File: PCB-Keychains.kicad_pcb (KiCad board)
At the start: 2 copper layers, 13 parts

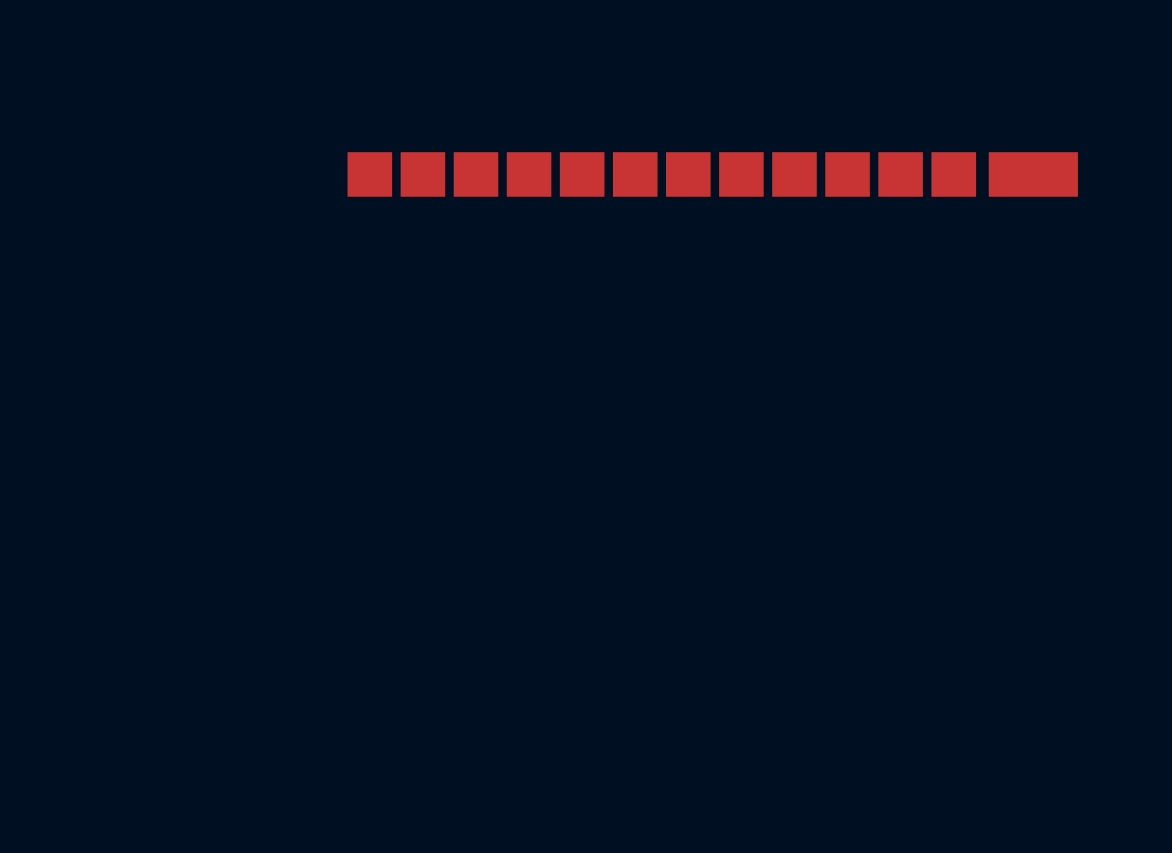
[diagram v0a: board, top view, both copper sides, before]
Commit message: Make tiny keychains, then realize it is too small
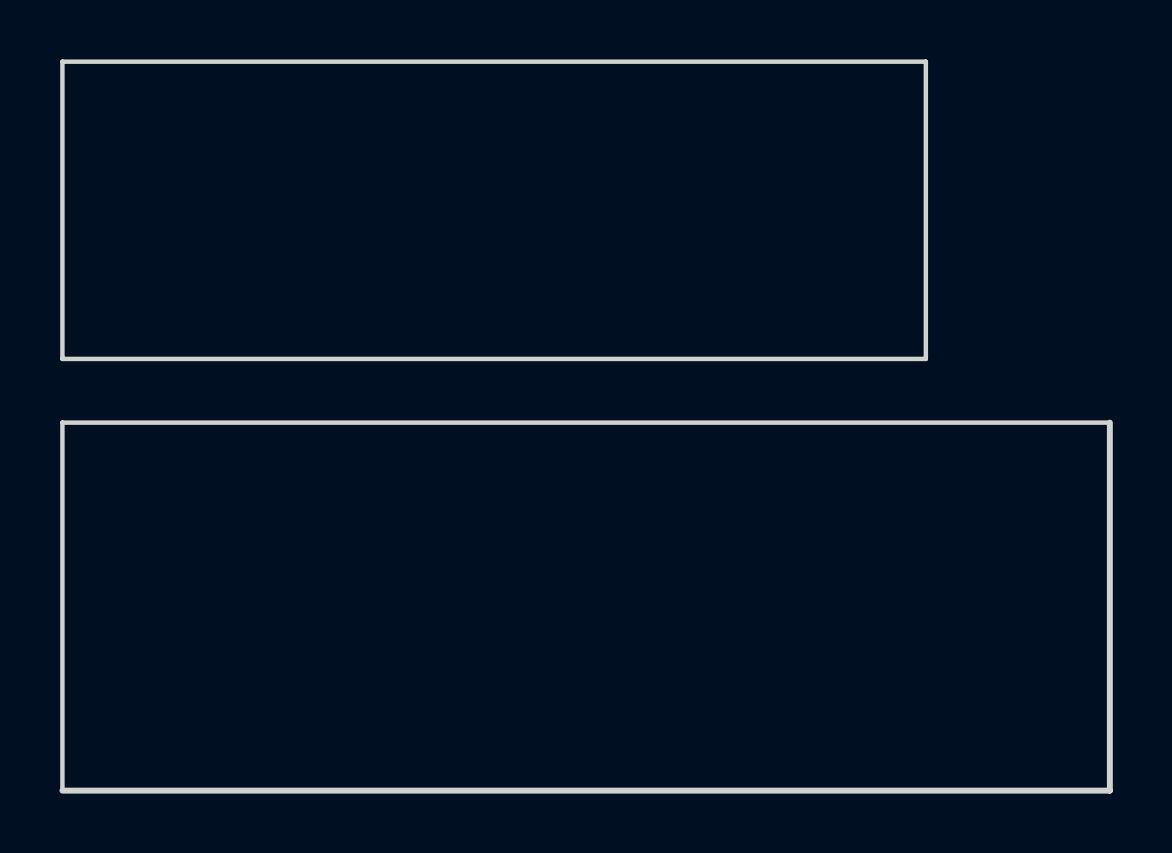
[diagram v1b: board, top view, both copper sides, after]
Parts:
- removed the REF** at (30.6, 21.7)
- removed the REF** at (46.7, 21.7)
- removed the REF** at (48.4, 21.7)
- removed the REF** at (50.2, 21.7)
- removed the REF** at (52.9, 21.7)
- removed the REF** at (32.4, 21.7)
- removed the REF** at (34.2, 21.7)
- removed the REF** at (35.9, 21.7)
- removed the REF** at (37.7, 21.7)
- removed the REF** at (39.5, 21.7)
- removed the REF** at (41.3, 21.7)
- removed the REF** at (43.1, 21.7)
- removed the REF** at (44.9, 21.7)
- added REF**: Pad-1U, locallib:Pad-1U, F.Cu at (42.4, 31.2)
- added REF**: Pad-1U, locallib:Pad-1U, F.Cu at (33.8, 31.2)
- added REF**: Pad-1U, locallib:Pad-1U, F.Cu at (34.3, 22.9)
- added REF**: Pad-1U, locallib:Pad-1U, F.Cu at (38.1, 22.9)
- added REF**: Pad-1U, locallib:Pad-1U, F.Cu at (40.0, 22.9)
- added REF**: Pad-1U, locallib:Pad-1U, F.Cu at (24.8, 22.9)
- added REF**: Pad-1U, locallib:Pad-1U, F.Cu at (30.5, 22.9)
- added REF**: Pad-1U, locallib:Pad-1U, F.Cu at (28.6, 22.9)
- added REF**: Pad-1U, locallib:Pad-1U, F.Cu at (26.7, 22.9)
- added REF**: Pad-1U, locallib:Pad-1U, F.Cu at (41.9, 22.9)
- added REF**: Pad-1U, locallib:Pad-1U, F.Cu at (43.8, 22.9)
- added REF**: Pad-1U, locallib:Pad-1U, F.Cu at (21.4, 19.1)
- added REF**: Pad-1U, locallib:Pad-1U, F.Cu at (37.6, 31.2)
- added REF**: Pad-1U, locallib:Pad-1U, F.Cu at (23.3, 19.1)
- added REF**: Pad-1U, locallib:Pad-1U, F.Cu at (25.2, 19.1)
- added REF**: Pad-1U, locallib:Pad-1U, F.Cu at (27.1, 19.1)
- added REF**: Pad-1U, locallib:Pad-1U, F.Cu at (29.1, 19.1)
- added REF**: Pad-1U, locallib:Pad-1U, F.Cu at (31.0, 19.1)
- added REF**: Pad-1U, locallib:Pad-1U, F.Cu at (32.9, 19.1)
- added REF**: Pad-1U, locallib:Pad-1U, F.Cu at (34.8, 19.1)
- added REF**: Pad-1U, locallib:Pad-1U, F.Cu at (36.7, 19.1)
- added REF**: Pad-1U, locallib:Pad-1U, F.Cu at (38.6, 19.1)
- added REF**: Pad-1U, locallib:Pad-1U, F.Cu at (40.5, 19.1)
- added REF**: Pad-1U, locallib:Pad-1U, F.Cu at (39.5, 31.2)
- added REF**: Pad-1U, locallib:Pad-1U, F.Cu at (42.4, 19.1)
- added REF**: Pad-1U, locallib:Pad-1U, F.Cu at (44.3, 19.1)
- added REF**: Pad-2U, locallib:Pad-2U, F.Cu at (47.1, 19.1)
- added REF**: Pad-1.5U, locallib:Pad-1.5U, F.Cu at (21.9, 21.0)
- added REF**: Pad-1U, locallib:Pad-1U, F.Cu at (24.3, 21.0)
- added REF**: Pad-1U, locallib:Pad-1U, F.Cu at (26.2, 21.0)
- added REF**: Pad-1U, locallib:Pad-1U, F.Cu at (28.1, 21.0)
- added REF**: Pad-1U, locallib:Pad-1U, F.Cu at (30.0, 21.0)
- added REF**: Pad-1U, locallib:Pad-1U, F.Cu at (31.9, 21.0)
- added REF**: Pad-1U, locallib:Pad-1U, F.Cu at (33.8, 21.0)
- added REF**: Pad-1U, locallib:Pad-1U, F.Cu at (29.1, 31.2)
- added REF**: Pad-1U, locallib:Pad-1U, F.Cu at (35.7, 21.0)
- added REF**: Pad-1U, locallib:Pad-1U, F.Cu at (37.6, 21.0)
- added REF**: Pad-1U, locallib:Pad-1U, F.Cu at (39.5, 21.0)
- added REF**: Pad-1U, locallib:Pad-1U, F.Cu at (41.4, 21.0)
- added REF**: Pad-1U, locallib:Pad-1U, F.Cu at (43.3, 21.0)
- added REF**: Pad-1U, locallib:Pad-1U, F.Cu at (45.2, 21.0)
- added REF**: Pad-1.5U, locallib:Pad-1.5U, F.Cu at (47.6, 21.0)
- added REF**: Pad-1.75U, locallib:Pad-1.75U, F.Cu at (22.1, 22.9)
- added REF**: Pad-2.25U, locallib:Pad-2.25U, F.Cu at (46.9, 22.9)
- added REF**: Pad-2.25U, locallib:Pad-2.25U, F.Cu at (22.6, 24.8)
- added REF**: Pad-1U, locallib:Pad-1U, F.Cu at (31.0, 31.2)
- added REF**: Pad-2.75U, locallib:Pad-2.75U, F.Cu at (46.4, 24.8)
- added REF**: Pad-1.5U, locallib:Pad-1.5U, F.Cu at (21.9, 26.7)
- added REF**: Pad-1U, locallib:Pad-1U, F.Cu at (24.3, 26.7)
- added REF**: Pad-1.5U, locallib:Pad-1.5U, F.Cu at (26.7, 26.7)
- added REF**: Pad-7U, locallib:Pad-7U, F.Cu at (34.8, 26.7)
- added REF**: Pad-1U, locallib:Pad-1U, F.Cu at (35.7, 31.2)
- added REF**: Pad-1U, locallib:Pad-1U, F.Cu at (21.4, 31.2)
- added REF**: Pad-1U, locallib:Pad-1U, F.Cu at (54.3, 41.2)
- added REF**: Pad-1U, locallib:Pad-1U, F.Cu at (52.4, 41.2)
- added REF**: Pad-1U, locallib:Pad-1U, F.Cu at (50.5, 41.2)
- added REF**: Pad-1U, locallib:Pad-1U, F.Cu at (44.3, 31.2)
- added REF**: Pad-1U, locallib:Pad-1U, F.Cu at (52.4, 39.3)
- added REF**: Pad-1U, locallib:Pad-1U, F.Cu at (54.3, 35.5)
- added REF**: Pad-1U, locallib:Pad-1U, F.Cu at (52.4, 35.5)
- added REF**: Pad-1U, locallib:Pad-1U, F.Cu at (50.5, 35.5)
- added REF**: Pad-1U, locallib:Pad-1U, F.Cu at (54.3, 33.6)
- added REF**: Pad-1U, locallib:Pad-1U, F.Cu at (52.4, 33.6)
- added REF**: Pad-1U, locallib:Pad-1U, F.Cu at (50.5, 33.6)
- added REF**: Pad-1U, locallib:Pad-1U, F.Cu at (44.3, 33.6)
- added REF**: Pad-1U, locallib:Pad-1U, F.Cu at (35.7, 35.5)
- added REF**: Pad-1U, locallib:Pad-1U, F.Cu at (31.9, 35.5)
- added REF**: Pad-1U, locallib:Pad-1U, F.Cu at (46.2, 31.2)
- added REF**: Pad-1U, locallib:Pad-1U, F.Cu at (33.8, 35.5)
- added REF**: Pad-1U, locallib:Pad-1U, F.Cu at (37.6, 35.5)
- added REF**: Pad-1U, locallib:Pad-1U, F.Cu at (39.5, 35.5)
- added REF**: Pad-1U, locallib:Pad-1U, F.Cu at (27.6, 39.3)
- added REF**: Pad-1U, locallib:Pad-1U, F.Cu at (33.3, 39.3)
- added REF**: Pad-1U, locallib:Pad-1U, F.Cu at (29.5, 39.3)
- added REF**: Pad-1U, locallib:Pad-1U, F.Cu at (41.0, 39.3)
- added REF**: Pad-1U, locallib:Pad-1U, F.Cu at (37.1, 39.3)
- added REF**: Pad-1U, locallib:Pad-1U, F.Cu at (42.9, 39.3)
- added REF**: Pad-1U, locallib:Pad-1U, F.Cu at (39.1, 39.3)
- added REF**: Pad-1U, locallib:Pad-1U, F.Cu at (48.1, 31.2)
- added REF**: Pad-1U, locallib:Pad-1U, F.Cu at (31.4, 39.3)
- added REF**: Pad-1U, locallib:Pad-1U, F.Cu at (25.7, 39.3)
- added REF**: Pad-1U, locallib:Pad-1U, F.Cu at (35.2, 39.3)
- added REF**: Pad-2.25U, locallib:Pad-2.25U, F.Cu at (22.6, 39.3)
- added REF**: Pad-2.75U, locallib:Pad-2.75U, F.Cu at (46.4, 39.3)
- added REF**: Pad-1U, locallib:Pad-1U, F.Cu at (24.3, 35.5)
- added REF**: Pad-1U, locallib:Pad-1U, F.Cu at (30.0, 35.5)
- added REF**: Pad-1U, locallib:Pad-1U, F.Cu at (28.1, 35.5)
- added REF**: Pad-1U, locallib:Pad-1U, F.Cu at (26.2, 35.5)
- added REF**: Pad-1U, locallib:Pad-1U, F.Cu at (27.1, 33.6)
- added REF**: Pad-1U, locallib:Pad-1U, F.Cu at (54.3, 31.2)
- added REF**: Pad-1U, locallib:Pad-1U, F.Cu at (32.9, 33.6)
- added REF**: Pad-1U, locallib:Pad-1U, F.Cu at (40.5, 33.6)
- added REF**: Pad-1U, locallib:Pad-1U, F.Cu at (31.0, 33.6)
- added REF**: Pad-1U, locallib:Pad-1U, F.Cu at (38.6, 33.6)
- added REF**: Pad-1U, locallib:Pad-1U, F.Cu at (36.7, 33.6)
- added REF**: Pad-1U, locallib:Pad-1U, F.Cu at (34.8, 33.6)
- added REF**: Pad-1U, locallib:Pad-1U, F.Cu at (29.1, 33.6)
- added REF**: Pad-1.5U, locallib:Pad-1.5U, F.Cu at (47.6, 35.5)
- added REF**: Pad-1U, locallib:Pad-1U, F.Cu at (45.2, 35.5)
- added REF**: Pad-1U, locallib:Pad-1U, F.Cu at (41.4, 35.5)
- added REF**: Pad-1U, locallib:Pad-1U, F.Cu at (52.4, 31.2)
- added REF**: Pad-1U, locallib:Pad-1U, F.Cu at (43.3, 35.5)
- added REF**: Pad-1.5U, locallib:Pad-1.5U, F.Cu at (21.9, 41.2)
- added REF**: Pad-1.5U, locallib:Pad-1.5U, F.Cu at (47.6, 41.2)
- added REF**: Pad-1.5U, locallib:Pad-1.5U, F.Cu at (42.9, 41.2)
- added REF**: Pad-1.5U, locallib:Pad-1.5U, F.Cu at (26.7, 41.2)
- added REF**: Pad-7U, locallib:Pad-7U, F.Cu at (34.8, 41.2)
- added REF**: Pad-1U, locallib:Pad-1U, F.Cu at (25.2, 33.6)
- added REF**: Pad-1U, locallib:Pad-1U, F.Cu at (42.4, 33.6)
- added REF**: Pad-1U, locallib:Pad-1U, F.Cu at (32.4, 37.4)
- added REF**: Pad-1U, locallib:Pad-1U, F.Cu at (24.8, 37.4)
- added REF**: Pad-1U, locallib:Pad-1U, F.Cu at (50.5, 31.2)
- added REF**: Pad-1U, locallib:Pad-1U, F.Cu at (41.9, 37.4)
- added REF**: Pad-1.75U, locallib:Pad-1.75U, F.Cu at (22.1, 37.4)
- added REF**: Pad-1U, locallib:Pad-1U, F.Cu at (40.0, 37.4)
- added REF**: Pad-1U, locallib:Pad-1U, F.Cu at (38.1, 37.4)
- added REF**: Pad-1U, locallib:Pad-1U, F.Cu at (34.3, 37.4)
- added REF**: Pad-1U, locallib:Pad-1U, F.Cu at (36.2, 37.4)
- added REF**: Pad-2.25U, locallib:Pad-2.25U, F.Cu at (46.9, 37.4)
- added REF**: Pad-1U, locallib:Pad-1U, F.Cu at (28.6, 37.4)
- added REF**: Pad-1U, locallib:Pad-1U, F.Cu at (30.5, 37.4)
- added REF**: Pad-1U, locallib:Pad-1U, F.Cu at (26.7, 37.4)
- added REF**: Pad-1U, locallib:Pad-1U, F.Cu at (27.1, 31.2)
- added REF**: Pad-1U, locallib:Pad-1U, F.Cu at (43.8, 37.4)
- added REF**: Pad-1U, locallib:Pad-1U, F.Cu at (23.3, 33.6)
- added REF**: Pad-1U, locallib:Pad-1U, F.Cu at (21.4, 33.6)
- added REF**: Pad-2U, locallib:Pad-2U, F.Cu at (47.1, 33.6)
- added REF**: Pad-1.5U, locallib:Pad-1.5U, F.Cu at (21.9, 35.5)
- added REF**: Pad-1.5U, locallib:Pad-1.5U, F.Cu at (42.9, 26.7)
- added REF**: Pad-1U, locallib:Pad-1U, F.Cu at (45.2, 26.7)
- added REF**: Pad-1.5U, locallib:Pad-1.5U, F.Cu at (47.6, 26.7)
- added REF**: Pad-1U, locallib:Pad-1U, F.Cu at (31.4, 24.8)
- added REF**: Pad-1U, locallib:Pad-1U, F.Cu at (41.0, 24.8)
- added REF**: Pad-1U, locallib:Pad-1U, F.Cu at (25.2, 31.2)
- added REF**: Pad-1U, locallib:Pad-1U, F.Cu at (39.1, 24.8)
- added REF**: Pad-1U, locallib:Pad-1U, F.Cu at (37.1, 24.8)
- added REF**: Pad-1U, locallib:Pad-1U, F.Cu at (33.3, 24.8)
- added REF**: Pad-1U, locallib:Pad-1U, F.Cu at (35.2, 24.8)
- added REF**: Pad-1U, locallib:Pad-1U, F.Cu at (27.6, 24.8)
- added REF**: Pad-1U, locallib:Pad-1U, F.Cu at (29.5, 24.8)
- added REF**: Pad-1U, locallib:Pad-1U, F.Cu at (25.7, 24.8)
- added REF**: Pad-1U, locallib:Pad-1U, F.Cu at (42.9, 24.8)
- added REF**: Pad-1U, locallib:Pad-1U, F.Cu at (36.2, 22.9)
- added REF**: Pad-1U, locallib:Pad-1U, F.Cu at (32.4, 22.9)
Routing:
- added copper zone on F.Cu, net (none)
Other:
- board outline added: 35.2 x 24.5 mm

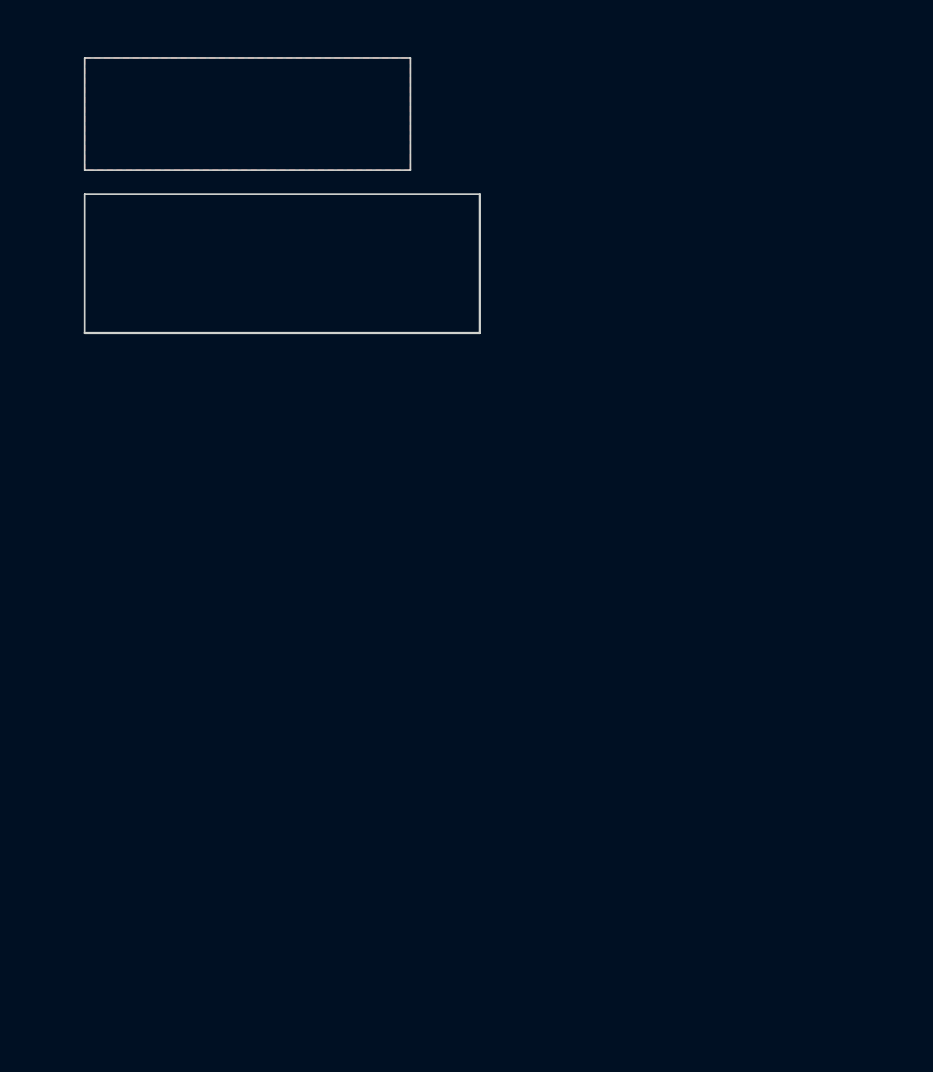
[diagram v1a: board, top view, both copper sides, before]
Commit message: Scale to 2x size, add 60%, TKL, and G80-1800
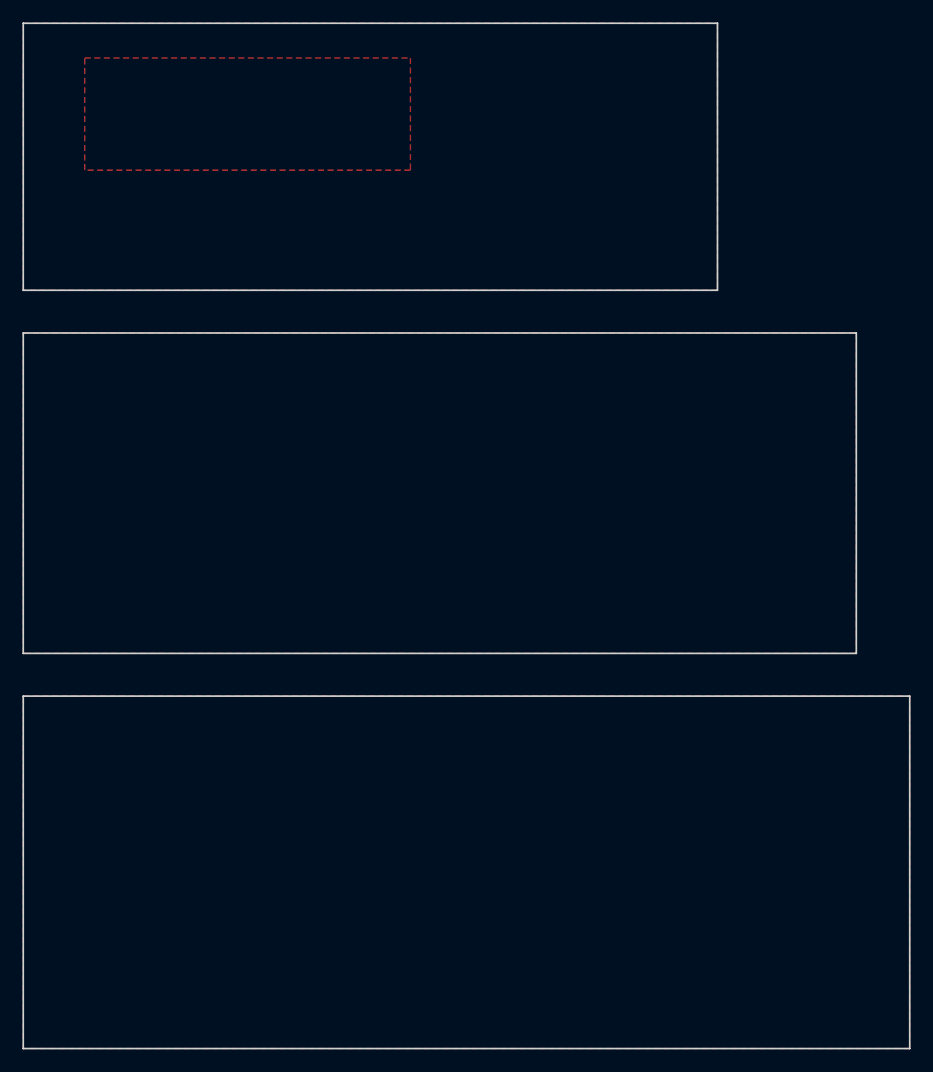
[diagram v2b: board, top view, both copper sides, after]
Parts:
- removed the REF** at (42.4, 31.2)
- removed the REF** at (33.8, 31.2)
- removed the REF** at (34.3, 22.9)
- removed the REF** at (38.1, 22.9)
- removed the REF** at (30.5, 22.9)
- removed the REF** at (26.7, 22.9)
- removed the REF** at (41.9, 22.9)
- removed the REF** at (21.4, 19.1)
- removed the REF** at (37.6, 31.2)
- removed the REF** at (23.3, 19.1)
- removed the REF** at (25.2, 19.1)
- removed the REF** at (27.1, 19.1)
- removed the REF** at (29.1, 19.1)
- removed the REF** at (31.0, 19.1)
- removed the REF** at (32.9, 19.1)
- removed the REF** at (34.8, 19.1)
- removed the REF** at (36.7, 19.1)
- removed the REF** at (38.6, 19.1)
- removed the REF** at (40.5, 19.1)
- removed the REF** at (39.5, 31.2)
- removed the REF** at (42.4, 19.1)
- removed the REF** at (44.3, 19.1)
- removed the REF** at (47.1, 19.1)
- removed the REF** at (21.9, 21.0)
- removed the REF** at (24.3, 21.0)
- removed the REF** at (26.2, 21.0)
- removed the REF** at (28.1, 21.0)
- removed the REF** at (30.0, 21.0)
- removed the REF** at (31.9, 21.0)
- removed the REF** at (33.8, 21.0)
- removed the REF** at (29.1, 31.2)
- removed the REF** at (35.7, 21.0)
- removed the REF** at (37.6, 21.0)
- removed the REF** at (39.5, 21.0)
- removed the REF** at (41.4, 21.0)
- removed the REF** at (43.3, 21.0)
- removed the REF** at (45.2, 21.0)
- removed the REF** at (47.6, 21.0)
- removed the REF** at (22.1, 22.9)
- removed the REF** at (46.9, 22.9)
- removed the REF** at (22.6, 24.8)
- removed the REF** at (31.0, 31.2)
- removed the REF** at (46.4, 24.8)
- removed the REF** at (21.9, 26.7)
- removed the REF** at (24.3, 26.7)
- removed the REF** at (26.7, 26.7)
- removed the REF** at (34.8, 26.7)
- removed the REF** at (35.7, 31.2)
- removed the REF** at (21.4, 31.2)
- removed the REF** at (54.3, 41.2)
- removed the REF** at (52.4, 41.2)
- removed the REF** at (50.5, 41.2)
- removed the REF** at (44.3, 31.2)
- removed the REF** at (52.4, 39.3)
- removed the REF** at (54.3, 35.5)
- removed the REF** at (52.4, 35.5)
- removed the REF** at (50.5, 35.5)
- removed the REF** at (54.3, 33.6)
- removed the REF** at (52.4, 33.6)
- removed the REF** at (50.5, 33.6)
- removed the REF** at (44.3, 33.6)
- removed the REF** at (35.7, 35.5)
- removed the REF** at (31.9, 35.5)
- removed the REF** at (46.2, 31.2)
- removed the REF** at (33.8, 35.5)
- removed the REF** at (37.6, 35.5)
- removed the REF** at (39.5, 35.5)
- removed the REF** at (27.6, 39.3)
- removed the REF** at (33.3, 39.3)
- removed the REF** at (29.5, 39.3)
- removed the REF** at (41.0, 39.3)
- removed the REF** at (37.1, 39.3)
- removed the REF** at (42.9, 39.3)
- removed the REF** at (39.1, 39.3)
- removed the REF** at (48.1, 31.2)
- removed the REF** at (31.4, 39.3)
- removed the REF** at (25.7, 39.3)
- removed the REF** at (35.2, 39.3)
- removed the REF** at (22.6, 39.3)
- removed the REF** at (46.4, 39.3)
- removed the REF** at (24.3, 35.5)
- removed the REF** at (30.0, 35.5)
- removed the REF** at (28.1, 35.5)
- removed the REF** at (26.2, 35.5)
- removed the REF** at (27.1, 33.6)
- removed the REF** at (54.3, 31.2)
- removed the REF** at (32.9, 33.6)
- removed the REF** at (40.5, 33.6)
- removed the REF** at (31.0, 33.6)
- removed the REF** at (38.6, 33.6)
- removed the REF** at (36.7, 33.6)
- removed the REF** at (34.8, 33.6)
- removed the REF** at (29.1, 33.6)
- removed the REF** at (47.6, 35.5)
- removed the REF** at (45.2, 35.5)
- removed the REF** at (41.4, 35.5)
- removed the REF** at (52.4, 31.2)
- removed the REF** at (43.3, 35.5)
- removed the REF** at (21.9, 41.2)
- removed the REF** at (47.6, 41.2)
- removed the REF** at (42.9, 41.2)
- removed the REF** at (26.7, 41.2)
- removed the REF** at (34.8, 41.2)
- removed the REF** at (25.2, 33.6)
- removed the REF** at (42.4, 33.6)
- removed the REF** at (32.4, 37.4)
- removed the REF** at (24.8, 37.4)
- removed the REF** at (50.5, 31.2)
- removed the REF** at (41.9, 37.4)
- removed the REF** at (22.1, 37.4)
- removed the REF** at (40.0, 37.4)
- removed the REF** at (38.1, 37.4)
- removed the REF** at (34.3, 37.4)
- removed the REF** at (36.2, 37.4)
- removed the REF** at (46.9, 37.4)
- removed the REF** at (28.6, 37.4)
- removed the REF** at (30.5, 37.4)
- removed the REF** at (26.7, 37.4)
- removed the REF** at (27.1, 31.2)
- removed the REF** at (43.8, 37.4)
- removed the REF** at (23.3, 33.6)
- removed the REF** at (21.4, 33.6)
- removed the REF** at (47.1, 33.6)
- removed the REF** at (21.9, 35.5)
- removed the REF** at (42.9, 26.7)
- removed the REF** at (45.2, 26.7)
- removed the REF** at (47.6, 26.7)
- removed the REF** at (31.4, 24.8)
- removed the REF** at (41.0, 24.8)
- removed the REF** at (25.2, 31.2)
- removed the REF** at (39.1, 24.8)
- removed the REF** at (37.1, 24.8)
- removed the REF** at (33.3, 24.8)
- removed the REF** at (35.2, 24.8)
- removed the REF** at (27.6, 24.8)
- removed the REF** at (29.5, 24.8)
- removed the REF** at (25.7, 24.8)
- removed the REF** at (42.9, 24.8)
- added REF**: Pad-1U, locallib:Pad-1U, F.Cu at (89.5, 82.9)
- added REF**: Pad-1U, locallib:Pad-1U, F.Cu at (85.7, 101.9)
- added REF**: Pad-1U, locallib:Pad-1U, F.Cu at (64.8, 46.7)
- added REF**: Pad-1U, locallib:Pad-1U, F.Cu at (72.4, 46.7)
- added REF**: Pad-1U, locallib:Pad-1U, F.Cu at (68.6, 46.7)
- added REF**: Pad-1U, locallib:Pad-1U, F.Cu at (61.0, 46.7)
- added REF**: Pad-1U, locallib:Pad-1U, F.Cu at (47.6, 46.7)
- added REF**: Pad-1U, locallib:Pad-1U, F.Cu at (55.2, 46.7)
- added REF**: Pad-1U, locallib:Pad-1U, F.Cu at (51.4, 46.7)
- added REF**: Pad-1U, locallib:Pad-1U, F.Cu at (43.8, 46.7)
- added REF**: Pad-1U, locallib:Pad-1U, F.Cu at (26.7, 46.7)
- added REF**: Pad-1U, locallib:Pad-1U, F.Cu at (19.1, 46.7)
- added REF**: Pad-1U, locallib:Pad-1U, F.Cu at (89.5, 94.3)
- added REF**: Pad-1U, locallib:Pad-1U, F.Cu at (77.2, 46.7)
- added REF**: Pad-1U, locallib:Pad-1U, F.Cu at (81.0, 46.7)
- added REF**: Pad-1U, locallib:Pad-1U, F.Cu at (84.8, 46.7)
- added REF**: Pad-1U, locallib:Pad-1U, F.Cu at (84.8, 66.7)
- added REF**: Pad-1U, locallib:Pad-1U, F.Cu at (81.0, 66.7)
- added REF**: Pad-1U, locallib:Pad-1U, F.Cu at (77.2, 66.7)
- added REF**: Pad-1U, locallib:Pad-1U, F.Cu at (81.0, 62.9)
- added REF**: Pad-1U, locallib:Pad-1U, F.Cu at (84.8, 55.2)
- added REF**: Pad-1U, locallib:Pad-1U, F.Cu at (81.0, 55.2)
- added REF**: Pad-1U, locallib:Pad-1U, F.Cu at (77.2, 55.2)
- added REF**: Pad-1U, locallib:Pad-1U, F.Cu at (78.1, 94.3)
- added REF**: Pad-1U, locallib:Pad-1U, F.Cu at (84.8, 51.4)
- added REF**: Pad-1U, locallib:Pad-1U, F.Cu at (81.0, 51.4)
- added REF**: Pad-1U, locallib:Pad-1U, F.Cu at (77.2, 51.4)
- added REF**: Pad-1.5U, locallib:Pad-1.5U, F.Cu at (71.4, 66.7)
- added REF**: Pad-1.5U, locallib:Pad-1.5U, F.Cu at (61.9, 66.7)
- added REF**: Pad-7U, locallib:Pad-7U, F.Cu at (45.7, 66.7)
- added REF**: Pad-1U, locallib:Pad-1U, F.Cu at (46.7, 62.9)
- added REF**: Pad-1U, locallib:Pad-1U, F.Cu at (27.6, 62.9)
- added REF**: Pad-2.25U, locallib:Pad-2.25U, F.Cu at (21.4, 62.9)
- added REF**: Pad-1.5U, locallib:Pad-1.5U, F.Cu at (20.0, 66.7)
- added REF**: Pad-1U, locallib:Pad-1U, F.Cu at (81.9, 94.3)
- added REF**: Pad-1U, locallib:Pad-1U, F.Cu at (61.9, 62.9)
- added REF**: Pad-1U, locallib:Pad-1U, F.Cu at (39.1, 62.9)
- added REF**: Pad-1U, locallib:Pad-1U, F.Cu at (58.1, 62.9)
- added REF**: Pad-1U, locallib:Pad-1U, F.Cu at (42.9, 62.9)
- added REF**: Pad-1U, locallib:Pad-1U, F.Cu at (35.2, 62.9)
- added REF**: Pad-1U, locallib:Pad-1U, F.Cu at (31.4, 62.9)
- added REF**: Pad-1.5U, locallib:Pad-1.5U, F.Cu at (29.5, 66.7)
- added REF**: Pad-1U, locallib:Pad-1U, F.Cu at (50.5, 62.9)
- added REF**: Pad-1U, locallib:Pad-1U, F.Cu at (54.3, 62.9)
- added REF**: Pad-2.75U, locallib:Pad-2.75U, F.Cu at (69.1, 62.9)
- added REF**: Pad-1U, locallib:Pad-1U, F.Cu at (85.7, 98.1)
- added REF**: Pad-1U, locallib:Pad-1U, F.Cu at (19.1, 51.4)
- added REF**: Pad-2U, locallib:Pad-2U, F.Cu at (70.5, 51.4)
- added REF**: Pad-1U, locallib:Pad-1U, F.Cu at (49.5, 51.4)
- added REF**: Pad-1U, locallib:Pad-1U, F.Cu at (48.6, 59.1)
- added REF**: Pad-1U, locallib:Pad-1U, F.Cu at (44.8, 59.1)
- added REF**: Pad-1U, locallib:Pad-1U, F.Cu at (56.2, 59.1)
- added REF**: Pad-1U, locallib:Pad-1U, F.Cu at (41.0, 59.1)
- added REF**: Pad-2.25U, locallib:Pad-2.25U, F.Cu at (70.0, 59.1)
- added REF**: Pad-1U, locallib:Pad-1U, F.Cu at (52.4, 59.1)
- added REF**: Pad-1U, locallib:Pad-1U, F.Cu at (60.0, 59.1)
- added REF**: Pad-1U, locallib:Pad-1U, F.Cu at (85.7, 94.3)
- added REF**: Pad-1U, locallib:Pad-1U, F.Cu at (37.1, 59.1)
- added REF**: Pad-1U, locallib:Pad-1U, F.Cu at (33.3, 59.1)
- added REF**: Pad-1U, locallib:Pad-1U, F.Cu at (63.8, 59.1)
- added REF**: Pad-1U, locallib:Pad-1U, F.Cu at (25.7, 59.1)
- added REF**: Pad-1U, locallib:Pad-1U, F.Cu at (29.5, 59.1)
- added REF**: Pad-1.75U, locallib:Pad-1.75U, F.Cu at (20.5, 59.1)
- added REF**: Pad-1U, locallib:Pad-1U, F.Cu at (32.4, 55.2)
- added REF**: Pad-1U, locallib:Pad-1U, F.Cu at (62.9, 55.2)
- added REF**: Pad-1U, locallib:Pad-1U, F.Cu at (24.8, 55.2)
- added REF**: Pad-1U, locallib:Pad-1U, F.Cu at (55.2, 55.2)
- added REF**: Pad-1U, locallib:Pad-1U, F.Cu at (81.9, 98.1)
- added REF**: Pad-1U, locallib:Pad-1U, F.Cu at (40.0, 55.2)
- added REF**: Pad-1.5U, locallib:Pad-1.5U, F.Cu at (71.4, 55.2)
- added REF**: Pad-1U, locallib:Pad-1U, F.Cu at (47.6, 55.2)
- added REF**: Pad-1U, locallib:Pad-1U, F.Cu at (59.1, 55.2)
- added REF**: Pad-1U, locallib:Pad-1U, F.Cu at (51.4, 55.2)
- added REF**: Pad-1U, locallib:Pad-1U, F.Cu at (28.6, 55.2)
- added REF**: Pad-1U, locallib:Pad-1U, F.Cu at (43.8, 55.2)
- added REF**: Pad-1U, locallib:Pad-1U, F.Cu at (36.2, 55.2)
- added REF**: Pad-1.5U, locallib:Pad-1.5U, F.Cu at (20.0, 55.2)
- added REF**: Pad-1U, locallib:Pad-1U, F.Cu at (66.7, 55.2)
- added REF**: Pad-1U, locallib:Pad-1U, F.Cu at (78.1, 98.1)
- added REF**: Pad-1U, locallib:Pad-1U, F.Cu at (61.0, 51.4)
- added REF**: Pad-1U, locallib:Pad-1U, F.Cu at (64.8, 51.4)
- added REF**: Pad-1U, locallib:Pad-1U, F.Cu at (30.5, 51.4)
- added REF**: Pad-1U, locallib:Pad-1U, F.Cu at (53.3, 51.4)
- added REF**: Pad-1U, locallib:Pad-1U, F.Cu at (57.1, 51.4)
- added REF**: Pad-1U, locallib:Pad-1U, F.Cu at (34.3, 51.4)
- added REF**: Pad-1U, locallib:Pad-1U, F.Cu at (45.7, 51.4)
- added REF**: Pad-1U, locallib:Pad-1U, F.Cu at (41.9, 51.4)
- added REF**: Pad-1U, locallib:Pad-1U, F.Cu at (38.1, 51.4)
- added REF**: Pad-1U, locallib:Pad-1U, F.Cu at (26.7, 51.4)
- added REF**: Pad-1U, locallib:Pad-1U, F.Cu at (89.5, 90.5)
- added REF**: Pad-1U, locallib:Pad-1U, F.Cu at (22.9, 51.4)
- added REF**: Pad-1U, locallib:Pad-1U, F.Cu at (66.7, 34.3)
- added REF**: Pad-1.5U, locallib:Pad-1.5U, F.Cu at (61.9, 34.3)
- added REF**: Pad-1.5U, locallib:Pad-1.5U, F.Cu at (71.4, 34.3)
- added REF**: Pad-1U, locallib:Pad-1U, F.Cu at (46.7, 30.5)
- added REF**: Pad-1U, locallib:Pad-1U, F.Cu at (42.9, 30.5)
- added REF**: Pad-1U, locallib:Pad-1U, F.Cu at (54.3, 30.5)
- added REF**: Pad-1U, locallib:Pad-1U, F.Cu at (39.1, 30.5)
- added REF**: Pad-1U, locallib:Pad-1U, F.Cu at (50.5, 30.5)
- added REF**: Pad-1U, locallib:Pad-1U, F.Cu at (58.1, 30.5)
- added REF**: Pad-1U, locallib:Pad-1U, F.Cu at (89.5, 86.7)
- added REF**: Pad-1U, locallib:Pad-1U, F.Cu at (35.2, 30.5)
- added REF**: Pad-1U, locallib:Pad-1U, F.Cu at (31.4, 30.5)
- added REF**: Pad-1U, locallib:Pad-1U, F.Cu at (61.9, 30.5)
- added REF**: Pad-1U, locallib:Pad-1U, F.Cu at (27.6, 30.5)
- added REF**: Pad-1U, locallib:Pad-1U, F.Cu at (33.3, 26.7)
- added REF**: Pad-1U, locallib:Pad-1U, F.Cu at (63.8, 26.7)
- added REF**: Pad-1U, locallib:Pad-1U, F.Cu at (25.7, 26.7)
- added REF**: Pad-1U, locallib:Pad-1U, F.Cu at (56.2, 26.7)
- added REF**: Pad-1U, locallib:Pad-1U, F.Cu at (41.0, 26.7)
- added REF**: Pad-1U, locallib:Pad-1U, F.Cu at (48.6, 26.7)
- added REF**: Pad-1U, locallib:Pad-1U, F.Cu at (89.5, 79.1)
- added REF**: Pad-1U, locallib:Pad-1U, F.Cu at (64.8, 86.7)
- added REF**: Pad-1U, locallib:Pad-1U, F.Cu at (60.0, 26.7)
- added REF**: Pad-1U, locallib:Pad-1U, F.Cu at (52.4, 26.7)
- added REF**: Pad-1U, locallib:Pad-1U, F.Cu at (29.5, 26.7)
- added REF**: Pad-1U, locallib:Pad-1U, F.Cu at (44.8, 26.7)
- added REF**: Pad-1U, locallib:Pad-1U, F.Cu at (37.1, 26.7)
- added REF**: Pad-1U, locallib:Pad-1U, F.Cu at (62.9, 22.9)
- added REF**: Pad-1U, locallib:Pad-1U, F.Cu at (66.7, 22.9)
- added REF**: Pad-1U, locallib:Pad-1U, F.Cu at (47.6, 22.9)
- added REF**: Pad-1U, locallib:Pad-1U, F.Cu at (59.1, 22.9)
- added REF**: Pad-1U, locallib:Pad-1U, F.Cu at (51.4, 22.9)
- added REF**: Pad-1U, locallib:Pad-1U, F.Cu at (51.4, 90.5)
- added REF**: Pad-1U, locallib:Pad-1U, F.Cu at (55.2, 22.9)
- added REF**: Pad-1U, locallib:Pad-1U, F.Cu at (49.5, 19.1)
- added REF**: Pad-1U, locallib:Pad-1U, F.Cu at (61.0, 19.1)
- added REF**: Pad-1U, locallib:Pad-1U, F.Cu at (64.8, 19.1)
- added REF**: Pad-1U, locallib:Pad-1U, F.Cu at (28.6, 90.5)
- added REF**: Pad-1U, locallib:Pad-1U, F.Cu at (57.1, 19.1)
- added REF**: Pad-1U, locallib:Pad-1U, F.Cu at (53.3, 19.1)
- added REF**: Pad-1U, locallib:Pad-1U, F.Cu at (34.3, 19.1)
- added REF**: Pad-1U, locallib:Pad-1U, F.Cu at (45.7, 19.1)
- added REF**: Pad-1U, locallib:Pad-1U, F.Cu at (41.9, 19.1)
- added REF**: Pad-1U, locallib:Pad-1U, F.Cu at (38.1, 19.1)
- added REF**: Pad-1U, locallib:Pad-1U, F.Cu at (26.7, 19.1)
- added REF**: Pad-1U, locallib:Pad-1U, F.Cu at (30.5, 19.1)
- added REF**: Pad-1U, locallib:Pad-1U, F.Cu at (19.1, 19.1)
- added REF**: Pad-1U, locallib:Pad-1U, F.Cu at (22.9, 19.1)
- added REF**: Pad-1U, locallib:Pad-1U, F.Cu at (43.8, 90.5)
- added REF**: Pad-2U, locallib:Pad-2U, F.Cu at (70.5, 19.1)
- added REF**: Pad-1.5U, locallib:Pad-1.5U, F.Cu at (20.0, 22.9)
- added REF**: Pad-1.5U, locallib:Pad-1.5U, F.Cu at (71.4, 22.9)
- added REF**: Pad-1.75U, locallib:Pad-1.75U, F.Cu at (20.5, 26.7)
- added REF**: Pad-2.25U, locallib:Pad-2.25U, F.Cu at (70.0, 26.7)
- added REF**: Pad-2.25U, locallib:Pad-2.25U, F.Cu at (21.4, 30.5)
- added REF**: Pad-2.75U, locallib:Pad-2.75U, F.Cu at (69.1, 30.5)
- added REF**: Pad-1.5U, locallib:Pad-1.5U, F.Cu at (20.0, 34.3)
- added REF**: Pad-1U, locallib:Pad-1U, F.Cu at (24.8, 34.3)
- added REF**: Pad-1.5U, locallib:Pad-1.5U, F.Cu at (29.5, 34.3)
- added REF**: Pad-1U, locallib:Pad-1U, F.Cu at (36.2, 90.5)
- added REF**: Pad-7U, locallib:Pad-7U, F.Cu at (45.7, 34.3)
- added REF**: Pad-1U, locallib:Pad-1U, F.Cu at (30.5, 46.7)
- added REF**: Pad-1U, locallib:Pad-1U, F.Cu at (34.3, 46.7)
- added REF**: Pad-1U, locallib:Pad-1U, F.Cu at (38.1, 46.7)
- added REF**: Pad-1.75U, locallib:Pad-1.75U, F.Cu at (67.2, 98.1)
- added REF**: Pad-2U, locallib:Pad-2U, F.Cu at (89.5, 100.0)
- added REF**: Pad-1.5U, locallib:Pad-1.5U, F.Cu at (20.0, 90.5)
- added REF**: Pad-1U, locallib:Pad-1U, F.Cu at (66.7, 90.5)
- added REF**: Pad-1U, locallib:Pad-1U, F.Cu at (61.0, 86.7)
- added REF**: Pad-1U, locallib:Pad-1U, F.Cu at (30.5, 86.7)
- added REF**: Pad-1U, locallib:Pad-1U, F.Cu at (41.9, 86.7)
- added REF**: Pad-1U, locallib:Pad-1U, F.Cu at (78.1, 79.1)
- added REF**: Pad-1U, locallib:Pad-1U, F.Cu at (53.3, 86.7)
- added REF**: Pad-1U, locallib:Pad-1U, F.Cu at (57.1, 86.7)
- added REF**: Pad-1U, locallib:Pad-1U, F.Cu at (34.3, 86.7)
- added REF**: Pad-1U, locallib:Pad-1U, F.Cu at (45.7, 86.7)
- added REF**: Pad-1U, locallib:Pad-1U, F.Cu at (38.1, 86.7)
- added REF**: Pad-1U, locallib:Pad-1U, F.Cu at (26.7, 86.7)
- added REF**: Pad-1U, locallib:Pad-1U, F.Cu at (22.9, 86.7)
- added REF**: Pad-1U, locallib:Pad-1U, F.Cu at (27.6, 79.1)
- added REF**: Pad-1U, locallib:Pad-1U, F.Cu at (43.8, 79.1)
- added REF**: Pad-1U, locallib:Pad-1U, F.Cu at (51.4, 79.1)
- added REF**: Pad-1U, locallib:Pad-1U, F.Cu at (81.9, 79.1)
- added REF**: Pad-1U, locallib:Pad-1U, F.Cu at (63.8, 79.1)
- added REF**: Pad-1U, locallib:Pad-1U, F.Cu at (56.2, 79.1)
- added REF**: Pad-1U, locallib:Pad-1U, F.Cu at (40.0, 79.1)
- added REF**: Pad-1U, locallib:Pad-1U, F.Cu at (67.6, 79.1)
- added REF**: Pad-1U, locallib:Pad-1U, F.Cu at (35.2, 79.1)
- added REF**: Pad-1U, locallib:Pad-1U, F.Cu at (47.6, 79.1)
- added REF**: Pad-1U, locallib:Pad-1U, F.Cu at (60.0, 79.1)
- added REF**: Pad-1U, locallib:Pad-1U, F.Cu at (31.4, 79.1)
- added REF**: Pad-1U, locallib:Pad-1U, F.Cu at (78.1, 86.7)
- added REF**: Pad-1U, locallib:Pad-1U, F.Cu at (81.9, 86.7)
- added REF**: Pad-1U, locallib:Pad-1U, F.Cu at (85.7, 82.9)
- added REF**: Pad-1U, locallib:Pad-1U, F.Cu at (73.3, 99.1)
- added REF**: Pad-1U, locallib:Pad-1U, F.Cu at (85.7, 90.5)
- added REF**: Pad-1U, locallib:Pad-1U, F.Cu at (23.8, 79.1)
- added REF**: Pad-1.5U, locallib:Pad-1.5U, F.Cu at (63.8, 101.9)
- added REF**: Pad-1U, locallib:Pad-1U, F.Cu at (77.2, 102.9)
- added REF**: Pad-1U, locallib:Pad-1U, F.Cu at (19.1, 79.1)
- added REF**: Pad-1U, locallib:Pad-1U, F.Cu at (73.3, 102.9)
- added REF**: Pad-1U, locallib:Pad-1U, F.Cu at (69.5, 102.9)
- added REF**: Pad-1U, locallib:Pad-1U, F.Cu at (81.9, 90.5)
- added REF**: Pad-1U, locallib:Pad-1U, F.Cu at (78.1, 90.5)
- added REF**: Pad-1U, locallib:Pad-1U, F.Cu at (85.7, 79.1)
- added REF**: Pad-1U, locallib:Pad-1U, F.Cu at (85.7, 86.7)
- added REF**: Pad-2.25U, locallib:Pad-2.25U, F.Cu at (21.4, 98.1)
- added REF**: Pad-1U, locallib:Pad-1U, F.Cu at (39.1, 98.1)
- added REF**: Pad-1U, locallib:Pad-1U, F.Cu at (42.9, 98.1)
- added REF**: Pad-1U, locallib:Pad-1U, F.Cu at (54.3, 98.1)
- added REF**: Pad-2.25U, locallib:Pad-2.25U, F.Cu at (70.0, 94.3)
- added REF**: Pad-2U, locallib:Pad-2U, F.Cu at (70.5, 86.7)
- added REF**: Pad-1U, locallib:Pad-1U, F.Cu at (24.8, 90.5)
- added REF**: Pad-1U, locallib:Pad-1U, F.Cu at (49.5, 86.7)
- added REF**: Pad-1U, locallib:Pad-1U, F.Cu at (44.8, 94.3)
- added REF**: Pad-1U, locallib:Pad-1U, F.Cu at (81.9, 82.9)
- added REF**: Pad-1U, locallib:Pad-1U, F.Cu at (55.2, 90.5)
- added REF**: Pad-1U, locallib:Pad-1U, F.Cu at (29.5, 94.3)
- added REF**: Pad-1U, locallib:Pad-1U, F.Cu at (37.1, 94.3)
- added REF**: Pad-1U, locallib:Pad-1U, F.Cu at (25.7, 94.3)
- added REF**: Pad-1U, locallib:Pad-1U, F.Cu at (40.0, 90.5)
- added REF**: Pad-7U, locallib:Pad-7U, F.Cu at (41.9, 101.9)
- added REF**: Pad-1U, locallib:Pad-1U, F.Cu at (41.0, 94.3)
- added REF**: Pad-1.5U, locallib:Pad-1.5U, F.Cu at (71.4, 90.5)
- added REF**: Pad-1U, locallib:Pad-1U, F.Cu at (46.7, 98.1)
- added REF**: Pad-1.5U, locallib:Pad-1.5U, F.Cu at (20.0, 101.9)
- added REF**: Pad-1U, locallib:Pad-1U, F.Cu at (78.1, 82.9)
- added REF**: Pad-1.75U, locallib:Pad-1.75U, F.Cu at (20.5, 94.3)
- added REF**: Pad-1U, locallib:Pad-1U, F.Cu at (31.4, 98.1)
- added REF**: Pad-1.5U, locallib:Pad-1.5U, F.Cu at (25.7, 101.9)
- added REF**: Pad-1U, locallib:Pad-1U, F.Cu at (19.1, 86.7)
- added REF**: Pad-1U, locallib:Pad-1U, F.Cu at (56.2, 94.3)
- added REF**: Pad-1U, locallib:Pad-1U, F.Cu at (52.4, 94.3)
- added REF**: Pad-1U, locallib:Pad-1U, F.Cu at (47.6, 90.5)
- added REF**: Pad-1U, locallib:Pad-1U, F.Cu at (32.4, 90.5)
- added REF**: Pad-1U, locallib:Pad-1U, F.Cu at (62.9, 90.5)
- added REF**: Pad-1U, locallib:Pad-1U, F.Cu at (60.0, 94.3)
- added REF**: Pad-1U, locallib:Pad-1U, F.Cu at (81.9, 101.9)
- added REF**: Pad-1U, locallib:Pad-1U, F.Cu at (35.2, 98.1)
- added REF**: Pad-1U, locallib:Pad-1U, F.Cu at (50.5, 98.1)
- added REF**: Pad-1U, locallib:Pad-1U, F.Cu at (48.6, 94.3)
- added REF**: Pad-1U, locallib:Pad-1U, F.Cu at (33.3, 94.3)
- added REF**: Pad-1.5U, locallib:Pad-1.5U, F.Cu at (58.1, 101.9)
- added REF**: Pad-1U, locallib:Pad-1U, F.Cu at (27.6, 98.1)
- added REF**: Pad-1U, locallib:Pad-1U, F.Cu at (61.9, 98.1)
- added REF**: Pad-1U, locallib:Pad-1U, F.Cu at (58.1, 98.1)
- added REF**: Pad-1U, locallib:Pad-1U, F.Cu at (63.8, 94.3)
- added REF**: Pad-1U, locallib:Pad-1U, F.Cu at (59.1, 90.5)
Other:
- board size 35.2 x 24.5 mm -> 79.1 x 91.4 mm
